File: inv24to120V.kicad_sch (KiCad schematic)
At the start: 191 parts, among them IC1 FSAM50SM60A, J1 0705530003, J10 Screw_Terminal_01x01, J12 Screw_Terminal_01x01, J2 Conn_01x02, J3 Conn_01x02, J7 Screw_Terminal_01x03, Q1 IRFZ44NPBF, Q2 IRFZ44NPBF, Q3 ZXTN2010ZTA, Q4 ZXTN2010ZTA, Q5 ZXTP2012ZTA, Q6 ZXTP2012ZTA, Q7 SUP53P06-20-E3, SW1 SW_DIP_x02, U1 ESP32-DEVKITC-32D, U10 FOD817A, U11 ACT45B-220-2P-TL003, U12 LM2576R-5.0, U13 FOD817A, U14 KIA7805AF, U15 FOD817A, U2 LM2576R-5.0, U3 ACS712ELCTR30AT, U4 ACS712ELCTR30AT, U6 ISO7340CDW, U7 ISO7340CDW, U8 AMC1300BDWVR, U9 TJA1040T

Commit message: sch design 1st done
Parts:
- removed BC17, BC18, BC19, BC20, BC21, BC22, BC24, BC25, BC26, BC27, BC31: 104/50V, mod:CAPC2012X95N, symbol CL21B104KBCNNND:CL21B104KBCNNND
- removed C15: 22uF/25V, Capacitor_SMD:C_1210_3225Metric_Pad1.33x2.70mm_HandSolder, symbol Device:C
- removed C24: 333, Capacitor_SMD:C_0805_2012Metric, symbol Device:C
- removed C25: 102, Capacitor_SMD:C_0805_2012Metric, symbol Device:C
- removed C29: 104, Capacitor_SMD:C_0805_2012Metric, symbol Device:C
- removed C3, C45, C48, C52, C55: 680uF/25V, Capacitor_SMD:CP_Elec_16x17.5, symbol MAL226099105E3:MAL226099105E3
- removed C37, C38: 103, Capacitor_SMD:C_0805_2012Metric, symbol Device:C
- removed C44: 470uF/25V, Capacitor_SMD:CP_Elec_10x12.5, symbol Device:C_Polarized
- removed D2, D6: SS26, mod:DIOM5127X229N, symbol Diode:1N5822
- removed D5: ES1F, mod:DIOM5027X244N, symbol Diode:1N5822
- removed D9: BYV29X-500, inv24VLib:TO507P1020X460X2000-2, symbol bead:D_Schottky
- removed IC1: FSAM50SM60A, inv24VLib:DIP-32, symbol FSAM50SM60A:FSAM50SM60A
- removed J1: 0705530003, genCtrlPCB_Lib:MOLEX_0705530039, symbol 0705530003:0705530003
- removed J10: Screw_Terminal_01x01, TerminalBlock_Wuerth:Wuerth_REDCUBE-THR_WP-THRBU_74650073_THR, symbol Connector:Screw_Terminal_01x01
- removed J2, J3: Conn_01x02, Connector_Molex:Molex_KK-396_A-41791-0002_1x02_P3.96mm_Vertical, symbol Connector_Generic:Conn_01x02
- removed J7: Screw_Terminal_01x03, TerminalBlock_Dinkle:TerminalBlock_Dinkle_DT-55-B01X-03_P10.00mm, symbol Connector:Screw_Terminal_01x03
- removed L6: L_Ferrite_Coupled_1423, Inductor_THT:L_CommonMode_Toroid_Vertical_L39.4mm_W20.3mm_Px15.24mm_Py22.86mm_Bourns_8100, symbol Device:L_Ferrite_Coupled_1423
- removed PC1, PC2: TLP115A, Package_SO:MFSOP6-5_4.4x3.6mm_P1.27mm, symbol Isolator:TLP137
- removed R10, R20, R21: 2K, Resistor_SMD:R_0805_2012Metric, symbol Device:R
- removed R11, R12, R13: 5.6, Resistor_SMD:R_2010_5025Metric_Pad1.40x2.65mm_HandSolder, symbol Device:R
- removed R14, R15, R16: 22, Resistor_SMD:R_2010_5025Metric_Pad1.40x2.65mm_HandSolder, symbol Device:R
- removed R22: 470, Resistor_SMD:R_0805_2012Metric, symbol Device:R
- removed R23: 390, Resistor_SMD:R_0805_2012Metric, symbol Device:R
- removed R24: 3.9K, Resistor_SMD:R_0805_2012Metric, symbol Device:R
- removed R25: 45, Resistor_SMD:R_0805_2012Metric, symbol Device:R
- removed R26, R27, R28: 4.7K, Resistor_SMD:R_0805_2012Metric, symbol Device:R
- removed R40: 10K, Resistor_SMD:R_0805_2012Metric_Pad1.20x1.40mm_HandSolder, symbol Device:R
- removed R42: 1K, Resistor_SMD:R_0805_2012Metric_Pad1.20x1.40mm_HandSolder, symbol Device:R
- removed R43: 120, Resistor_SMD:R_0805_2012Metric_Pad1.20x1.40mm_HandSolder, symbol Device:R
- removed R44: 4.7K, Resistor_SMD:R_0805_2012Metric_Pad1.20x1.40mm_HandSolder, symbol Device:R
- removed R45: 220, Resistor_SMD:R_0805_2012Metric_Pad1.20x1.40mm_HandSolder, symbol Device:R
- removed R46: 470, Resistor_SMD:R_0805_2012Metric_Pad1.20x1.40mm_HandSolder, symbol Device:R
- removed R47: 0, Resistor_SMD:R_0805_2012Metric_Pad1.20x1.40mm_HandSolder, symbol Device:R
- removed R48, R49: 60, Resistor_SMD:R_0805_2012Metric_Pad1.20x1.40mm_HandSolder, symbol Device:R
- removed R53: 1k, Resistor_SMD:R_0805_2012Metric_Pad1.20x1.40mm_HandSolder, symbol Device:R
- removed TP1, TP2, TP3, TP4: TestPoint, TestPoint:TestPoint_Loop_D2.50mm_Drill1.0mm, symbol Connector:TestPoint
- removed U10: FOD817A, inv24VLib:PDIP4GW_709AH_ONS-M, symbol Isolator:PC817
- removed U11: ACT45B-220-2P-TL003, genCtrlPCB_Lib:FIL_ACT45B-220-2P-TL003, symbol ACT45B-220-2P-TL003:ACT45B-220-2P-TL003
- removed U12, U2: LM2576R-5.0, genCtrlPCB_Lib:VREG_TPS79625KTTR, symbol LM2576S-12_NOPB:LM2576S-12_NOPB
- removed U14: KIA7805AF, Package_TO_SOT_SMD:ATPAK-2, symbol Regulator_Linear:L7805
- removed U3, U4: ACS712ELCTR30AT, inv24VLib:SOIC127P600X175-8N, symbol ACS712ELCTR30AT:ACS712ELCTR30AT
- removed U5: ~, Library:ewDCDC24_1505d, symbol ewDCDC_24_1508d:con24_1508d
- removed U6, U7: ISO7340CDW, inv24VLib:SOIC127P1030X265-16N, symbol ISO7340CDW:ISO7340CDW
- removed U8: AMC1300BDWVR, inv24VLib:SOIC127P1150X280-8N, symbol AMC1300BDWVR:AMC1300BDWVR
- removed U9: TJA1040T, genCtrlPCB_Lib:SOIC127P600X175-8N, symbol TJA1040T:TJA1040T
- removed ZD1, ZD2, ZD3: ZMM55C27, Diode_SMD:D_MiniMELF, symbol Diode:ZMMxx
- added BX5: 2.5A/0.8K, mod:BLM31KN102BH1L, symbol BLM31KN801SH1L:BLM31KN801SH1L
- added C10: 102, Capacitor_SMD:C_0805_2012Metric, symbol Device:C
- added C11, C16, C18, C19, C3, C7, C9: 2.2uF/50V, Capacitor_SMD:C_1206_3216Metric_Pad1.33x1.80mm_HandSolder, symbol Device:C
- added C15, C17: 680uF/25V, Capacitor_SMD:CP_Elec_16x17.5, symbol MAL226099105E3:MAL226099105E3
- added C20: 473, Capacitor_SMD:C_0805_2012Metric, symbol Device:C
- added C23: 4.7p, Capacitor_SMD:C_0805_2012Metric, symbol Device:C
- added D10, D11, D12, D14: BAT48J, Diode_SMD:D_SOD-323_HandSoldering, symbol Diode:1N5822
- added D13, D15, D16: 15V/1W, Diode_SMD:D_SMA_Handsoldering, symbol Device:D_Zener_Small
- added F3, F4, F5: 7A/350V, Fuse:Fuse_2920_7451Metric_Pad2.10x5.45mm_HandSolder, symbol Device:Fuse_Small
- added FL1: ACT45B-510-2P-TL003, ACT45B1012PTL003, symbol ACT45B-510-2P-TL003:ACT45B-510-2P-TL003
- added IC1: MCP2551-E_SN, SOIC127P600X175-8N, symbol MCP2551-E_SN:MCP2551-E_SN
- added IC2: ISO7221AQDRQ1, SOIC127P600X175-8N, symbol ISO7221AQDRQ1:ISO7221AQDRQ1
- added J1: 70543-0003, mod:SHDR4W97P0X254_1X4_1271X660X1143P, symbol 70543-0003:70543-0003
- added J2, J3: 70543-0001, mod:SHDR2W64P0X254_1X2_737X660X1181P, symbol 70543-0001:70543-0001
- added J4: Screw_Terminal_01x03, TerminalBlock_Dinkle:TerminalBlock_Dinkle_DT-55-B01X-03_P10.00mm, symbol Connector:Screw_Terminal_01x03
- added J5: BR-120, TerminalBlock_Wuerth:Wuerth_REDCUBE-THR_WP-THRBU_74650073_THR, symbol Connector:Screw_Terminal_01x01
- added LED1, LED2: LTST-C170GKT, LEDC2012X120N, symbol LTST-C170GKT:LTST-C170GKT
- added PS1: NTE0505MC, mod:NTE0505MC, symbol NTE0505MC:NTE0505MC
- added Q8: STGIF7CH60TS-L, mod:STGIB20M60TSL, symbol STGIB20M60TS-L:STGIB20M60TS-L
- added R10, R26, R27, R28: 1.0K, Resistor_SMD:R_1206_3216Metric_Pad1.30x1.75mm_HandSolder, symbol Device:R_Small
- added R11: 12K, Resistor_SMD:R_1206_3216Metric_Pad1.30x1.75mm_HandSolder, symbol Device:R_Small
- added R12: 10K, Resistor_SMD:R_1206_3216Metric_Pad1.30x1.75mm_HandSolder, symbol Device:R_Small
- added R13, R14, R15, R16: 120, mod:RESC2012X65N, symbol RC2012F100CS:RC2012F_SQR
- added R20, R21: 0, mod:RESC2012X65N, symbol RC2012F100CS:RC2012F_SQR
- added R22, R23: 470, mod:RESC2012X65N, symbol RC2012F100CS:RC2012F_SQR
- added R51: 4.7K, Resistor_SMD:R_1206_3216Metric_Pad1.30x1.75mm_HandSolder, symbol Device:R_Small
- added U2: LM2576D2T-15G, genCtrlPCB_Lib:VREG_TPS79625KTTR, symbol lm2576:LM2576D2T-15G
- added U3: LM2576-3.3WU, genCtrlPCB_Lib:VREG_TPS79625KTTR, symbol lm2576:LM2576S-3.3
- added U4: LM2576D2TR4-5G, genCtrlPCB_Lib:VREG_TPS79625KTTR, symbol lm2576:LM2576D2T-5G
- added Z2, Z3: SMAJ40AHE3_A/H, mod:DIOM5027X244N, symbol SMAJ4745AQ-TP:SMAJ4745AQ-TP
- C13, C14: value 22uF/25V -> 104; footprint Capacitor_SMD:C_1210_3225Metric_Pad1.33x2.70mm_HandSolder -> Capacitor_SMD:C_0805_2012Metric; Cost 402 -> 20; Manufacturer_Part_Number CL32B226KAJNNNE -> CL21B104KBCNNNE; Mouser Part Number 187-CL32B226KAJNNNE -> 187-CL21B104KBCNNNE; Mouser Price/Stock https://www.mouser.kr/ProductDetail/Samsung-Electro-Mechani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 -> https://www.mouser.co.uk/ProductDetail/Samsung-Electro-Mech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
- C21: value 102 -> 4.7p; Cost (none) -> 20; Manufacturer_Name (none) -> SAMSUNG; Manufacturer_Part_Number (none) -> CL21B047PKBCNNNE; Mouser Part Number (none) -> 187-CL21B473KBCNNNE; Mouser Price/Stock (none) -> https://www.mouser.co.uk/ProductDetail/Samsung-Electro-Mech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
- C8: value 102 -> 2.2uF/50V; footprint Capacitor_SMD:C_0805_2012Metric -> Capacitor_SMD:C_1206_3216Metric_Pad1.33x1.80mm_HandSolder; Cost 20 -> 402; Manufacturer_Part_Number CL21B102KBCNNNE -> CL31A225KB9LNNC; Mouser Part Number 187-CL21B104KBCNNNE -> 187-CL31A225KB9LNNC; Mouser Price/Stock https://www.mouser.co.uk/ProductDetail/Samsung-Electro-Mech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 -> https://www.mouser.kr/ProductDetail/Samsung-Electro-Mechani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
- D1: value SS26 -> BYV29X-600; footprint mod:DIOM5127X229N -> mod:TO507P1020X460X2000-2; Cost 500 -> 900; Height 2.29 -> 0; Manufacturer_Name Vishay -> WeEn Semiconductors; Manufacturer_Part_Number SS26SHE3_B/H -> BYV29X-600,127; Mouser Part Number 78-SS26SHE3_B/H -> 771-BYV29X-600127; Mouser Price/Stock https://www.mouser.co.uk/ProductDetail/Vishay-General-Semic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 -> https://www.mouser.kr/ProductDetail/WeEn-Semiconductors/BYV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
- D3, D4: value ES1F -> SS26; footprint mod:DIOM5027X244N -> mod:DIOM5127X229N; Manufacturer_Name onsemi / Fairchild -> Vishay; Manufacturer_Part_Number ES1F -> SS26SHE3_B/H; Mouser Part Number 512-ES1F -> 78-SS26SHE3_B/H; Mouser Price/Stock https://www.mouser.kr/ProductDetail/onsemi-Fairchild/ES1F?q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 -> https://www.mouser.co.uk/ProductDetail/Vishay-General-Semic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
- F1, F2: footprint inv24VLib:FUSE_3544-2 -> mod:FUSE_3544-2; Availability In Stock -> (none); Check_prices https://www.snapeda.com/parts/3544-2/Keystone+Electronics/v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 -> (none); Cost (none) -> 1000; Height (none) -> 9.02mm; MANUFACTURER Keystone -> (none); MAXIMUM_PACKAGE_HEIGHT 9.02mm -> (none); MF Keystone Electronics -> (none); MP 3544-2 -> (none); Manufacturer_Name (none) -> Keystone Electronics; Manufacturer_Part_Number (none) -> 3544-2; Mouser Part Number (none) -> 534-3544-2; Mouser Price/Stock (none) -> https://www.mouser.kr/ProductDetail/Keystone-Electronics/35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; PARTREV C -> (none); Package None -> (none); Price None -> (none); Purchase-URL https://www.snapeda.com/api/url_track_click_mouser/?unipart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 -> (none); SNAPEDA_PN 3544-2 -> (none); STANDARD Manufacturer Recommendations -> (none); SnapEDA_Link https://www.snapeda.com/parts/3544-2/Keystone+Electronics/v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 -> (none)
- H1, H2, H3, H4, H5, H6: now left out of the parts list
- J12: value Screw_Terminal_01x01 -> BR-120; Cost (none) -> 360; Manufacturer_Name (none) -> 비룡전자; Manufacturer_Part_Number (none) -> BR-120; Mouser Part Number (none) -> https://www.devicemart.co.kr : BR-120; Mouser Price/Stock (none) -> https://www.devicemart.co.kr/goods/view?no=1232631
- L1, L2, L3, L5: footprint Inductor_SMD:L_12x12mm_H8mm -> mod:INDPM120120X600N; Cost (none) -> 1700; Manufacturer_Name (none) -> Wurth Elektronik; Manufacturer_Part_Number (none) -> 7447706101; Mouser Part Number (none) -> 710-7447706101; Mouser Price/Stock (none) -> https://www.mouser.kr/ProductDetail/Wurth-Elektronik/744770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
- L4: footprint inv24VLib:IND_HCTI-10-20.0 -> mod:IND_HCTI-10-20.0; Cost (none) -> 4300; Manufacturer_Name (none) -> 서광전자; Manufacturer_Part_Number (none) -> RING COIL 21파이(22uH); Mouser Part Number (none) -> https://www.devicemart.co.kr/goods/view?no=31729; Mouser Price/Stock (none) -> https://www.devicemart.co.kr/goods/view?no=31729
- Q7: Cost (none) -> 3800
- R7, R8, R9: value 2K -> 0.08/2W; footprint Resistor_SMD:R_0805_2012Metric -> Resistor_SMD:R_2816_7142Metric_Pad3.20x4.45mm_HandSolder; Cost (none) -> 1140; Height (none) -> 0.95; Manufacturer_Name (none) -> Vishay / Dale; Manufacturer_Part_Number (none) -> WSL2816R0800FEH; Mouser Part Number (none) -> 71-WSL2816R0800FEH; Mouser Price/Stock (none) -> https://www.mouser.kr/ProductDetail/Vishay-Dale/WSL2816R080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
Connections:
- net +8VP_IN is gone; now on net +5P: BC3.1
- net +BATT is gone; now on net +5P: L5.2
- net UH1 is gone; now on net PWM0_H: R29.1
- net UL1 is gone; now on net PWM0_L: R32.1
- net VH1 is gone; now on net PWM1_H: R30.1
- net VL1 is gone; now on net PWM1_L: R33.1
- net VTH_IPM is gone; now on net GNDPWR: BX1.2
- net WH1 is gone; now on net PWM2_H: R31.1
- net WL1 is gone; now on net PWM2_L: R34.1
- net +15V: now also BC23.1, BC7.1, C2.1 (+), C6.1 (+), L1.2, C11.1, C16.1, Q8.13 (VCCL), Q8.8 (VCCH), U2.4 (FB); no longer BC14.1
- net +24V: now also BC10.1, BC11.1, BC13.1, BC14.1, D1.1 (K), U2.5 (ON/OFF), U3.5 (ON/OFF), U4.5 (ON/OFF)
- net +3.3V: now also BC16.1, L3.2, C15.1 (+), D14.1 (K), IC2.1 (VCC1), Q8.26 (T1), R12.2, R22.1, R23.1, U3.4 (FB); no longer BC15.1, BC7.1
- net +5P: now also BC15.1, C19.1, IC1.3 (VDD), IC2.8 (VCC2), J1.1, J2.1, J3.1; no longer BC1.1
- net +5V: now also BC1.1, BX2.2, L2.2, C17.1 (+), C18.1, PS1.3 (+VIN_), U4.4 (FB); no longer BC16.1, BC4.2, BC5.1, BX1.1, C2.1 (+), L1.2
- net +5VP: no longer BC13.1, BC6.1, BC8.1, L2.2
- net GND: now also BC1.2, BC10.2, BC11.2, BC13.2, BC14.2, BC28.2, BC9.2, BX1.1, BX3.1, BX4.2, C13.2, C14.1, D3.2 (A), D4.2 (A), F2.2_1, F2.2_2, RV1.2, RV2.1, C10.2, C15.2 (-), C17.2 (-), C18.2, IC2.4 (GND1), PS1.1 (-VIN), Q8.16 (GND_2), Q8.9 (GND_1), R11.2, R51.1, U2.1 (VIN), U2.3 (GND), U2.6 (GND), U3.1 (VIN), U3.3 (GND), U3.6 (GND), U4.1 (VIN), U4.3 (GND), U4.6 (GND); no longer BC15.2, BC4.1, BC5.2, BC7.2, BX2.1, C21.1, C8.2, R9.1
- net GND1: now also BC15.2, C21.2, C19.2, C20.2, C23.2, IC1.2 (VSS), IC1.8 (RS), IC2.5 (GND2), J1.2, PS1.7 (-VOUT), Z2.2 (A), Z3.2 (A); no longer BC1.2
- net GND2: now also BC7.2, C11.2, C16.2; no longer BC13.2, BC14.2, BC6.2, BC8.2, BX3.1
- net GNDPWR: now also BC8.2, R7.2, R8.2, R9.2
- net IN_UH: now also Q8.5 (HINU)
- net IN_UL: now also Q8.10 (LINU)
- net IN_VH: now also Q8.6 (HINV)
- net IN_VL: now also Q8.11 (LINV)
- net IN_WH: now also Q8.7 (HINW)
- net IN_WL: now also Q8.12 (LINW)
- net I_Uphase: no longer R7.1, R9.2
- net I_Vphase: no longer R8.1
- net TEMPERATURE_IPM: now also C10.1, D14.2 (A), Q8.17 (TSO); no longer BX4.1
- net VDC_sensor: now also BC9.1, BX5.1; no longer C21.2
- net at Q7.2 (D): now also BC28.1, D1.2 (A), RT1.2
- net at L5.1: now also PS1.8 (+VOUT)
- net at R18.1, R19.2: now also BC8.1, BX5.2
- net at D7.1 (K), L1.1: now also U2.2 (OUT)
- net VBOOT_V: now reaches C8.1
- net VBOOT_V: now also BC5.1, D13.1 (K), Q8.3 (VBOOTV)
- net CIN: now reaches C5.1
- net CIN: now also Q8.15 (CIN), R28.1, R51.2
- net SD: now reaches C14.2
- net SD: now also Q8.14 (~{SD}/OD), R12.1; no longer BC10.2
- net at L2.1: now also D4.1 (K), U4.2 (OUT)
- net at R62.2: now also J3.2
- net at F2.1_2: now also F2.1_1, J5.1 (Pin_1)
- net at L3.1: now also D3.1 (K), U3.2 (OUT); no longer D1.1 (K)
- net at R60.2: now also J2.2
- removed net 15V_H_IN: BC23.1, C6.1 (+), D1.2 (A)
- new net: R15.1, R16.1, R21.2
- new net: C20.1, IC1.5 (VREF), R13.2, R14.2, R15.2, R16.2
- new net: FL1.3, J1.4, Z2.1 (K)
- new net: LED1.2 (A), R23.2
- new net: D10.1 (K), D11.1 (K), D12.1 (K), R28.2
- new net: D10.2 (A), R10.1
- new net: Q8.18 (NW), R10.2, R9.1
- new net: C23.1, FL1.2, IC1.6 (CANL), R21.1
- new net: Q8.19 (NV), R26.2, R8.1
- new net: Q8.20 (NU), R27.2, R7.1
- new net: D12.2 (A), R27.1
- new net: D11.2 (A), R26.1
- new net: IC2.3 (INB), LED2.1 (K)
- new net: LED2.2 (A), R22.2
- new net: IC2.2 (OUTA), LED1.1 (K)
- new net: IC1.1 (TXD), IC2.6 (OUTB)
- new net: IC1.4 (RXD), IC2.7 (INA)
- new net: C21.1, FL1.1, IC1.7 (CANH), R20.1
- new net: BX2.1, C3.1
- new net: F4.2, J4.2 (Pin_2)
- new net: F3.2, J4.1 (Pin_1)
- new net: R13.1, R14.1, R20.2
- new net: BX4.1, C3.2
- new net: FL1.4, J1.3, Z3.1 (K)
- new net: F5.2, J4.3 (Pin_3)
- new net PHASE_U: BC4.2, C7.2, D15.2 (A), F3.1, Q8.23 (U)
- new net PHASE_V: BC5.2, C8.2, D13.2 (A), F4.1, Q8.22 (V)
- new net PHASE_W: BC6.2, C9.2, D16.2 (A), F5.1, Q8.21 (W)
- new net T2: C13.1, Q8.25 (T2), R11.1
- new net VBOOT_U: BC4.1, C7.1, D15.1 (K), Q8.2 (VBOOTU)
- new net VBOOT_W: BC6.1, C9.1, D16.1 (K), Q8.4 (VBOOTW)
- new net V_DC_LINK: Q8.24 (P)
- no-connect marks 13 -> 11
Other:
- moved on the sheet: BC23, BC29, BC30, BX3, C12, C2, C22, C27, C28, C30, C31, C56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

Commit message: start place component
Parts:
- removed BC28, BC29, BC30: 104/50V, mod:CAPC2012X95N, symbol CL21B104KBCNNND:CL21B104KBCNNND
- removed D15, D16: 15V/1W, Diode_SMD:D_SMA_Handsoldering, symbol Device:D_Zener_Small
- removed R1, R2, R57, R58: 10, Resistor_SMD:R_0805_2012Metric_Pad1.20x1.40mm_HandSolder, symbol Device:R
- removed R12: 10K, Resistor_SMD:R_1206_3216Metric_Pad1.30x1.75mm_HandSolder, symbol Device:R_Small
- removed R17, R18: 1M/2W, Resistor_SMD:R_1206_3216Metric_Pad1.30x1.75mm_HandSolder, symbol Device:R
- removed R19, R50: 1K, Resistor_SMD:R_0805_2012Metric_Pad1.20x1.40mm_HandSolder, symbol Device:R
- removed R29, R30, R31, R32, R33, R34: 100, Resistor_SMD:R_0805_2012Metric, symbol Device:R
- removed R3, R38, R4: 10K, Resistor_SMD:R_0805_2012Metric_Pad1.20x1.40mm_HandSolder, symbol Device:R
- removed R35, R36, R37: 4.7K, Resistor_SMD:R_0805_2012Metric, symbol Device:R
- removed R39: 2K, Resistor_SMD:R_0805_2012Metric_Pad1.20x1.40mm_HandSolder, symbol Device:R
- removed R41, R5, R6: 100, Resistor_SMD:R_0805_2012Metric_Pad1.20x1.40mm_HandSolder, symbol Device:R
- removed R60, R62: 470, Resistor_SMD:R_0805_2012Metric, symbol Device:R
- removed R61, R63, R64, R65: 10K, Resistor_SMD:R_0805_2012Metric, symbol Device:R
- removed U13: FOD817A, inv24VLib:PDIP4GW_709AH_ONS-M, symbol Isolator:PC817
- added BC17, BC18, BC19: 104/50V, mod:CAPC2012X95N, symbol CL21B104KBCNNND:CL21B104KBCNNND
- added D2, D5: 15V/1W, Diode_SMD:D_SMA_Handsoldering, symbol Device:D_Zener_Small
- added R1, R2, R24, R25: 10, Resistor_SMD:R_0805_2012Metric_Pad1.20x1.40mm_HandSolder, symbol RC2012F100CS:RC2012F_SQR
- added R12, R3, R38, R4, R40, R42, R43, R44: 10K, Resistor_SMD:R_0805_2012Metric_Pad1.20x1.40mm_HandSolder, symbol RC2012F100CS:RC2012F_SQR
- added R17, R18, R41, R46: 500K/3216, Resistor_SMD:R_1206_3216Metric_Pad1.30x1.75mm_HandSolder, symbol RC2012F100CS:RC2012F_SQR
- added R19, R47: 1.0K, Resistor_SMD:R_1206_3216Metric_Pad1.30x1.75mm_HandSolder, symbol Device:R_Small
- added R29, R30, R31, R32, R33, R34, R45, R5, R6: 100, Resistor_SMD:R_0805_2012Metric_Pad1.20x1.40mm_HandSolder, symbol RC2012F100CS:RC2012F_SQR
- added R35: 2.0K, Resistor_SMD:R_1206_3216Metric_Pad1.30x1.75mm_HandSolder, symbol Device:R_Small
- added R48, R49: 470, Resistor_SMD:R_0805_2012Metric_Pad1.20x1.40mm_HandSolder, symbol RC2012F100CS:RC2012F_SQR
- added U5: FOD817A3SD, mod:PDIP4GW_709AH_ONS-M, symbol Isolator:PC817
- BC1, BC10, BC11, BC12, BC13, BC14, BC15, BC16, BC2, BC23, BC3, BC4, BC5, BC6, BC7, BC8, BC9: Cost (none) -> 80; Height 0.95 -> (none)
- BX1, BX2, BX3, BX4, BX5: Cost (none) -> 500; Height 1.8 -> (none)
- C1, C4: Cost (none) -> 5000
- C15, C17, C2, C6: Height 17.5 -> (none)
- C22: Height 35 -> (none)
- D1, D8: Height 0 -> (none)
- D10, D11, D12, D14, D3, D4, D7: Height 2.29 -> (none)
- D13: Cost (none) -> 900
- F1, F2: Height 9.02mm -> (none)
- FL1: Height 3 -> (none)
- IC1, IC2: Height 1.75 -> (none)
- J1: Height 11.43 -> (none)
- J2, J3: Height 11.81 -> (none)
- LED1, LED2: Height 1.2 -> (none)
- PS1: Height 6.85 -> (none)
- Q1, Q2: Cost (none) -> 1470; Manufacturer_Name (none) -> Infineon Technologies; Manufacturer_Part_Number (none) -> IRFZ44NPBF; Mouser Part Number (none) -> 942-IRFZ44NPBF; Mouser Price/Stock (none) -> https://www.mouser.kr/ProductDetail/Infineon-Technologies/I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
- Q3, Q4: Cost (none) -> 1100; Manufacturer_Name (none) -> Diodes Incorporated; Manufacturer_Part_Number (none) -> ZXTN2010ZTA; Mouser Part Number (none) -> 522-ZXTN2010ZTA; Mouser Price/Stock (none) -> https://www.mouser.kr/ProductDetail/Diodes-Incorporated/ZXT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
- Q5, Q6: Cost (none) -> 1147; Manufacturer_Name (none) -> Diodes Incorporated; Manufacturer_Part_Number (none) -> ZXTP2012ZTA; Mouser Part Number (none) -> 522-ZXTP2012ZTA; Mouser Price/Stock (none) -> https://www.mouser.kr/ProductDetail/Diodes-Incorporated/ZXT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
- Q7: Height 4.65 -> (none)
- Q8: Height 6 -> (none)
- R10, R11, R26, R27, R28, R51, R7, R8, R9: Height 0.95 -> (none)
- R13, R14, R15, R16, R20, R21, R22, R23: footprint mod:RESC2012X65N -> Resistor_SMD:R_0805_2012Metric_Pad1.20x1.40mm_HandSolder
- RT1: Cost (none) -> 1400; Height 37 -> (none)
- RV1, RV2, RV3: footprint inv24VLib:VAR_ERZ-VF2M560 -> mod:VAR_ERZ-VF2M560; Cost (none) -> 1600; MANUFACTURER Panasonic -> (none); MAXIMUM_PACKAGE_HEIGHT 3.5mm -> (none); Manufacturer_Name (none) -> Panasonic; Manufacturer_Part_Number (none) -> ERZ-VF2M560; Mouser Part Number (none) -> 667-ERZ-VF2M560; Mouser Price/Stock (none) -> https://www.mouser.kr/ProductDetail/Panasonic/ERZ-VF2M560?q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; PARTREV 14-Dec-20 -> (none); STANDARD Manufacturer Recommendations -> (none)
- SW1: Availability In Stock -> (none); Check_prices https://www.snapeda.com/parts/418117270902/Wurth+Elektronik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 -> (none); Cost (none) -> 1600; DATASHEET-URL https://www.we-online.com/catalog/datasheet/418117270902.pdf -> (none); Description_1 Dip Switch SPST 2 Position Through Hole Slide (Standard) Ac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 -> (none); MF Würth Elektronik -> (none); MP 418117270902 -> (none); Manufacturer_Name (none) -> Wurth Elektronik; Manufacturer_Part_Number (none) -> 418117270902; Mouser Part Number (none) -> 710-418117270902; Mouser Price/Stock (none) -> https://www.mouser.kr/ProductDetail/Wurth-Elektronik/418117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; PART-NUMBER 418117270902 -> (none); PINS 2 -> (none); Package None -> (none); Price None -> (none); QTY 82 -> (none); SnapEDA_Link https://www.snapeda.com/parts/418117270902/Wurth+Elektronik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 -> (none)
- TR1: Cost (none) -> 100000; Manufacturer_Name (none) -> DLT Korea; Manufacturer_Part_Number (none) -> PQ5050-24-300-6PV; Mouser Part Number (none) -> Nop; Mouser Price/Stock (none) -> Nop
- U1: Cost (none) -> 40000; MANUFACTURER Espressif Systems -> (none); MAXIMUM_PACKAGE_HEIGHT N/A -> (none); Manufacturer_Name (none) -> DLT Korea; Manufacturer_Part_Number (none) -> DLT-dspModule_241; Mouser Part Number (none) -> Nop; Mouser Price/Stock (none) -> Nop; PARTREV V4 -> (none); SNAPEDA_PN ESP32-DEVKITC-32D -> (none); STANDARD Manufacturer Recommendations -> (none)
- U15: value FOD817A -> FOD817A3SD; footprint inv24VLib:PDIP4GW_709AH_ONS-M -> mod:PDIP4GW_709AH_ONS-M; Cost (none) -> 800; Manufacturer_Name (none) -> onsemi / Fairchild; Manufacturer_Part_Number (none) -> 호: FOD817A3SD; Mouser Part Number (none) -> 512-FOD817A3SD; Mouser Price/Stock (none) -> https://www.mouser.kr/ProductDetail/onsemi-Fairchild/FOD817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
- U2, U3, U4: footprint genCtrlPCB_Lib:VREG_TPS79625KTTR -> mod:KTT0005B
- Z1: Cost (none) -> 450; Height 1.35 -> (none)
- Z2, Z3: Height 2.44 -> (none)
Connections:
- net +24V: now also R35.2
- net +3.3V: now also R12.1, R43.1, R44.1
- net +5V: now also BC18.1; no longer BC1.1
- net CIN: now also U1.J3-2 (IO23)
- net DIN_A: now also BC1.1, R43.2, U5.4
- net DIN_B: now also BC17.1, R44.2
- net FAULT_IPM: now also U1.J3-10 (IO5); no longer U1.J3-2 (IO23)
- net GND: now also C12.2, C27.2, C28.2, C30.2, C31.2, C62.2, RV3.1, BC17.2, BC18.2, BC19.2, R3.2, R34.2, R4.2, R47.2, U5.3; no longer RV2.1
- net GND1: now also R40.2, R42.2, U5.2
- net GND2: no longer C12.2, C27.2, C28.2, C30.2, C31.2, C62.2
- net GNDPWR: now also R19.2
- net IN_UH: now also R29.1
- net IN_UL: now also R45.1
- net IN_VH: now also R30.1
- net IN_VL: now also R32.1
- net IN_WH: now also R31.1
- net IN_WL: now also R33.1
- net PHASE_U: now also D5.2 (A)
- net PHASE_W: now also D2.2 (A)
- net PWM0_H: now also R29.2
- net PWM0_L: now also R45.2
- net PWM1_H: now also R30.2
- net PWM1_L: now also R32.2
- net PWM2_H: now also R31.2
- net PWM2_L: now also R33.2
- net PWM_A: now also R5.2
- net PWM_B: now also R6.2
- net SD: now also R12.2
- net VBOOT_U: now also D5.1 (K)
- net VBOOT_W: now also D2.1 (K)
- net VBUS: now also R41.1
- net VDC_IN: now also R38.1
- net at F1.2_1, F1.2_2, RT1.1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: now also RV2.1; no longer RV3.1
- net at D1.2 (A), Q7.2 (D), RT1.2: now also BC19.1
- net at BC8.1, BX5.2: now also R19.1, R46.1
- net at Q7.1 (G), Z1.2 (A): now also R47.1
- net at Q4.1 (B), Q6.1 (B): now also R6.1
- net at Q4.3 (E): now also R2.2
- net CAN_TX: now reaches IC2.3 (INB), LED2.1 (K)
- net CAN_RX: now reaches IC2.2 (OUTA), LED1.1 (K)
- net at J2.2: now also R48.1
- net at Q2.1 (G): now also R2.1, R24.1, R4.1
- net at U15.1: now also R42.1, R49.2
- net at Q5.3 (E): now also R25.2
- net at Q1.1 (G): now also R1.1, R25.1, R3.1
- net at Q3.1 (B), Q5.1 (B): now also R5.1
- net at Q3.3 (E): now also R1.2
- net at Q6.3 (E): now also R24.2
- net at J3.2: now also R49.1
- net SCI_RXD renamed CAN_RXD
- net SCI_TXD renamed CAN_TXD
- new net: R18.1, R46.2
- new net: R34.1, R35.1, R38.2
- new net: R17.2, R18.2
- new net: R40.1, R48.2, U5.1
- new net: R17.1, R41.2
- no-connect marks 11 -> 10
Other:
- moved on the sheet: C27, C28, C62, R51

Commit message: add pause cause mati argue
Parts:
- added C24, C25: 220uF/50V, Capacitor_SMD:CP_Elec_16x17.5, symbol MAL226099105E3:MAL226099105E3
- added D6: BYV29X-600, Package_TO_SOT_THT:TO-220-2_Horizontal_TabUp, symbol Diode:1N5822
- D8: footprint mod:TO507P1020X460X2000-2 -> Package_TO_SOT_THT:TO-220-2_Horizontal_TabUp
- F3, F4, F5: footprint Fuse:Fuse_2920_7451Metric_Pad2.10x5.45mm_HandSolder -> Fuse:Fuse_2512_6332Metric_Pad1.52x3.35mm_HandSolder
- IC1, IC2: footprint SOIC127P600X175-8N -> mod:SOIC127P600X175-8N
- Q7: footprint mod:TO254P465X1028X1931-3P -> Package_TO_SOT_THT:TO-220-3_Horizontal_TabUp
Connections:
- net ANALOG_CMD is gone; now on net TEMPERATURE_IPM: U1.J2-6 (IO35)
- net GND2 is gone; now on net GND: BC23.2, BC7.2, C11.2, C16.2, C6.2 (-)
- net V_DC_LINK is gone; now on net VBUS: Q8.24 (P)
- net +24V: now also C24.1 (+), C25.1 (+)
- net +3.3V: no longer U1.J2-1 (3V3)
- net +5V: now also BX2.1, C3.1; no longer BC18.1, BX2.2, C18.1, PS1.3 (+VIN_)
- net 300V_OUT1: now also D6.2 (A)
- net GND: now also BX4.1, C3.2, C24.2 (-), C25.2 (-); no longer BC18.2, BX4.2, C18.2, PS1.1 (-VIN)
- net T2: now also U1.J2-7 (IO32)
- net TEMPERATURE_IPM: no longer U1.J2-7 (IO32)
- net at D8.1 (K), L4.2: now also D6.1 (K)
- new net: BC18.1, BX2.2, C18.1, PS1.3 (+VIN_)
- new net: BC18.2, BX4.2, C18.2, PS1.1 (-VIN)
- no-connect marks 10 -> 13

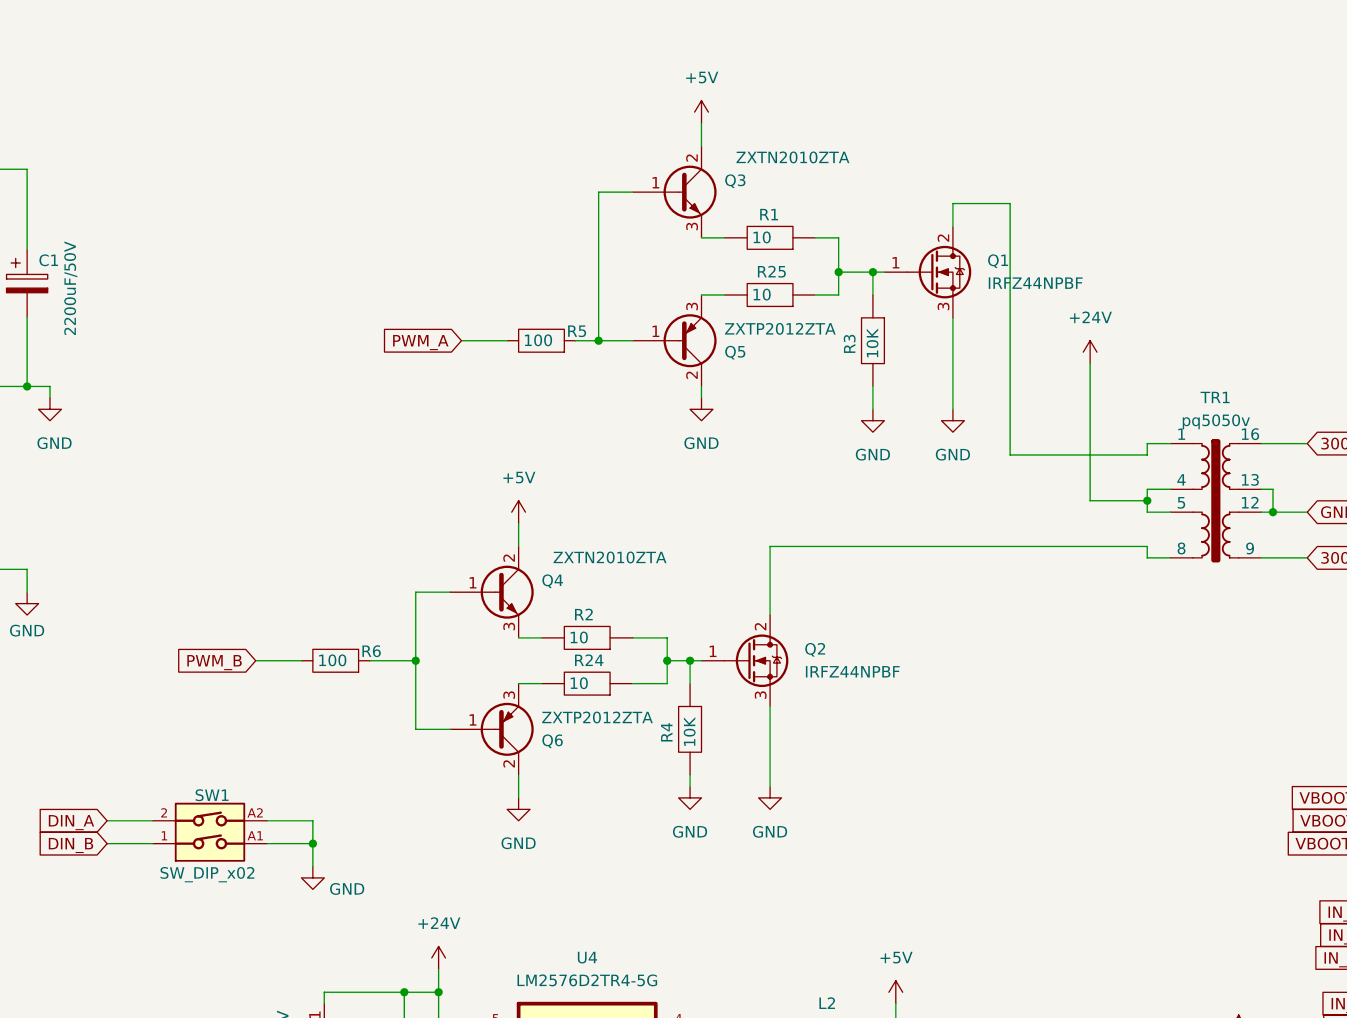
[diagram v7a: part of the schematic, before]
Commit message: finish routing next add copper for power
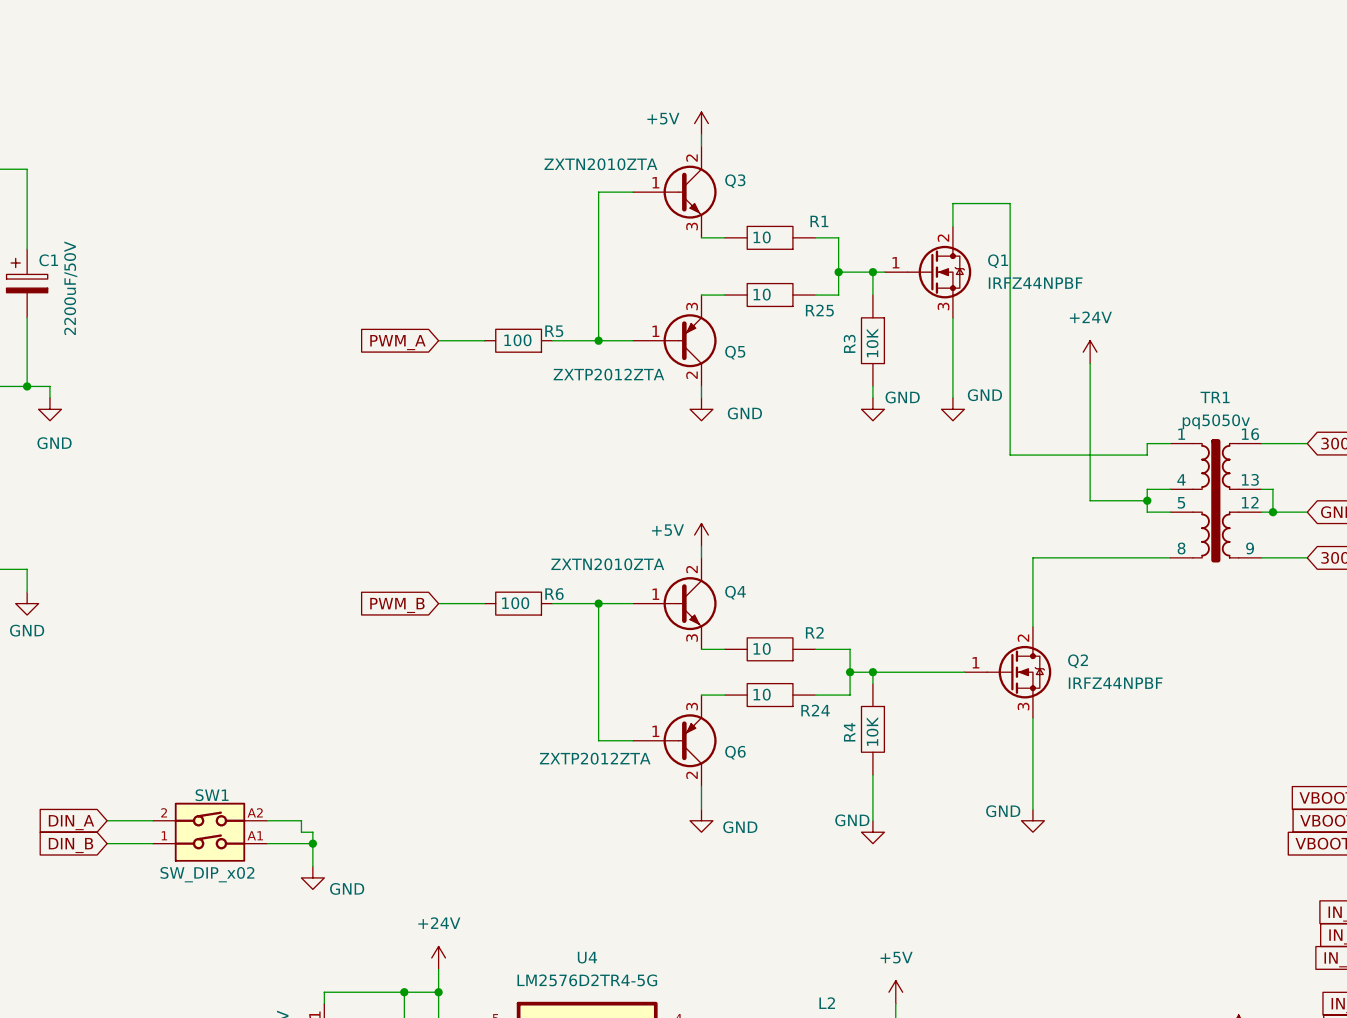
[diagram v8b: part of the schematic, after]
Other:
- moved on the sheet: Q2, Q4, Q6, R2, R24, R4, R5, R6
